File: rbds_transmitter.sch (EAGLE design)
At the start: 36 parts, among them IC1 MAX1551, IC2 TPS61030, IC3 MCP4812, Q1 P-Ch, SW1 FSMSM, U3 ATMEGA328, X1 HD44780LCD-1602, Y1 16Mhz

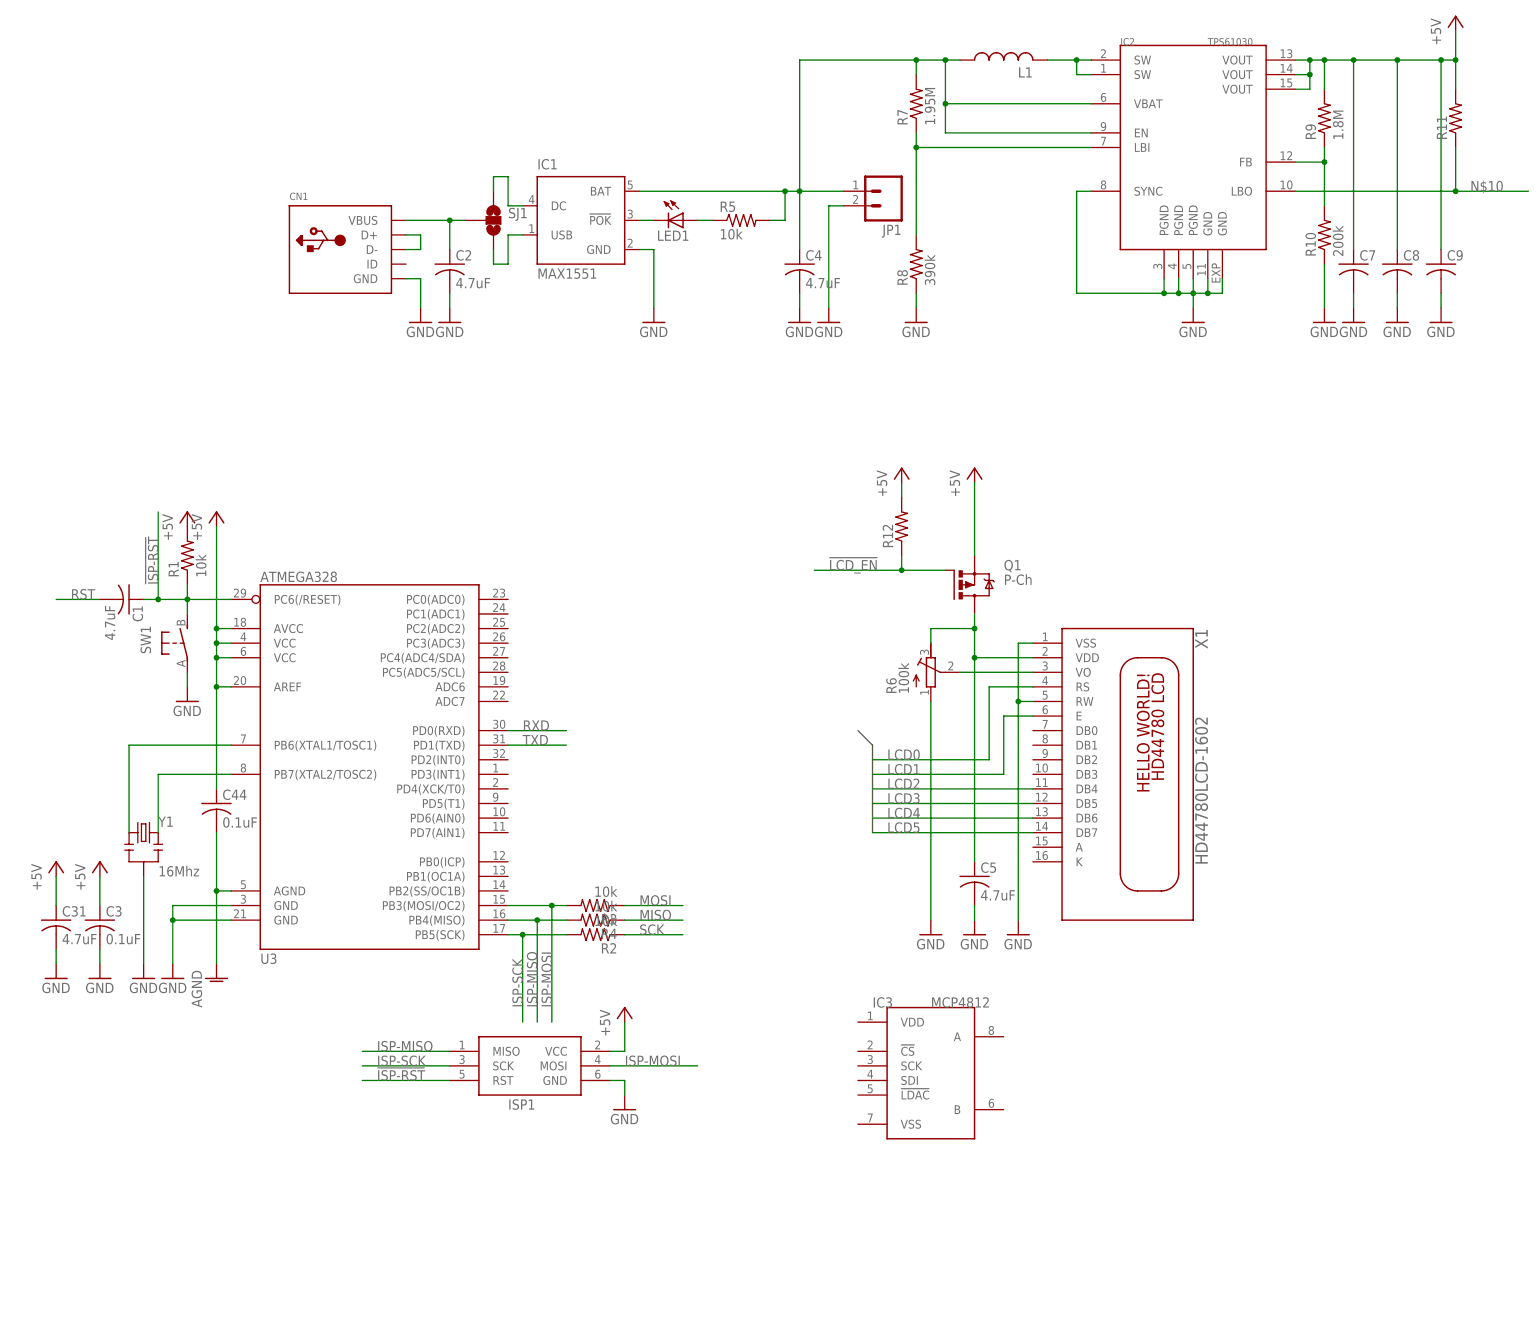
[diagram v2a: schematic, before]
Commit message: wiring up dac
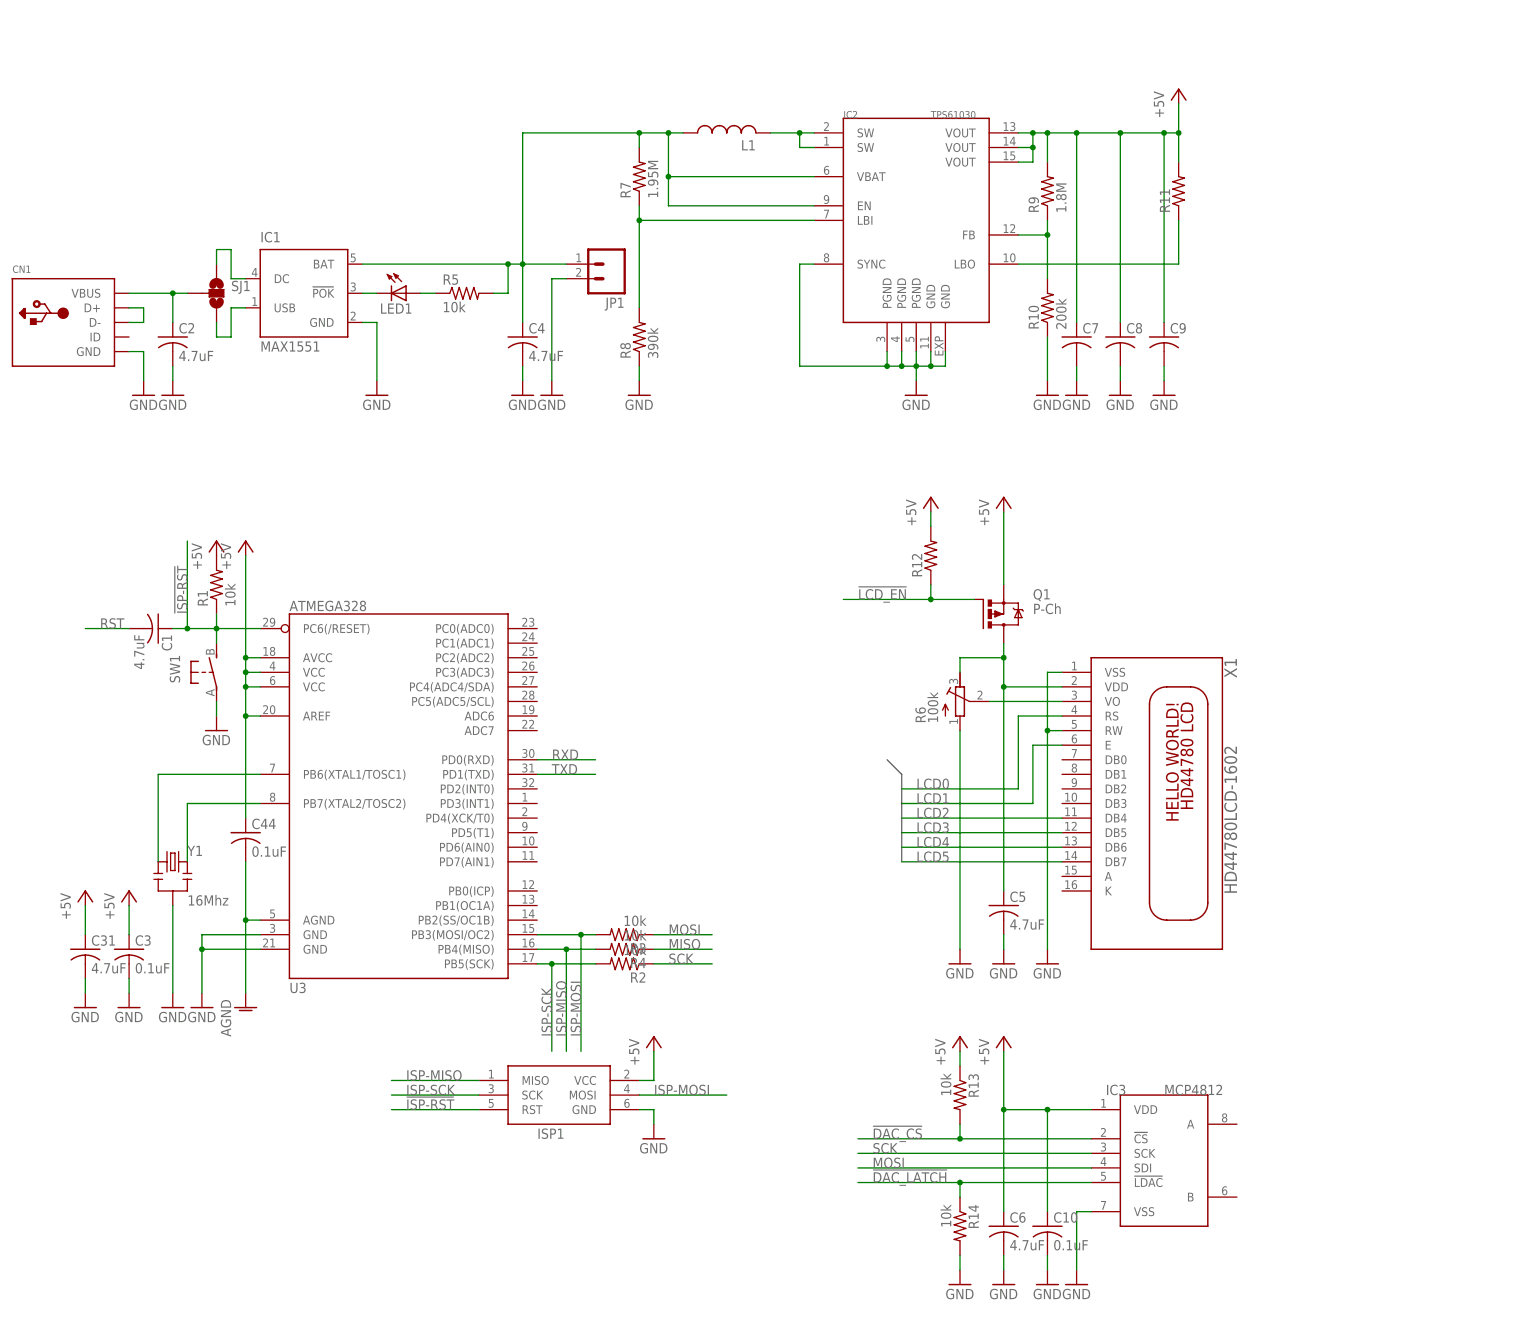
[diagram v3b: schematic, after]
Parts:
- added C10: 0.1uF, adafruit:C-USC1206
- added C6: 4.7uF, adafruit:C-USC1206
- added R13, R14: 10k, adafruit:R-US_R1206
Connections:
- new net !DAC_CS: IC3.!CS, R13.2
- new net !DAC_LATCH: IC3.!LDAC, R14.1
- net +5V: now also C10.1, C6.1, IC3.VDD, R13.1
- net GND: now also C10.2, C6.2, IC3.VSS, R14.2
- net MOSI: now also IC3.SDI
- net SCK: now also IC3.SCK
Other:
- moved on the sheet: C1, C2, C3, C31, C4, C44, C5, C7, C8, C9, CN1, IC1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

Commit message: added diode ring mixer
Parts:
- added C11: (no value), adafruit:C-USC1206
- added D1, D2, D3, D4: (no value), dp_devices:DIODE-SOD-123
- added JP2: (no value), sparkfun:M02PTH
- added R15: (no value), adafruit:R-US_R1206
- added TR1, TR2: (no value), inductor-neosid:SM-T4-2T
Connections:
- new net N$14: D1.A, D4.C, TR1.2
- new net N$16: D1.C, D2.A, TR2.2
- new net N$18: D2.C, D3.A, TR1.4
- new net N$19: TR1.3
- new net N$20: R15.1, TR1.1
- new net N$21: C11.1, TR2.1
- new net N$22: C11.2
- new net N$3: D3.C, D4.A, TR2.4
- net GND: now also JP2.2, TR1.5, TR2.3, TR2.5
- net N$11: now also JP2.1

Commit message: opamps
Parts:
- added IC4: OPA4743UA, linear:OPA4743UA
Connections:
- net N$22: now also IC4A.+IN
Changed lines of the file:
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@@
 <grid distance="0.1" unitdist="inch" unit="inch" style="lines" multiple="1" display="no" altdistance="0.01" altunitdist="inch" altunit="inch"/>
 <layers>
-<layer number="1" name="Top" color="4" fill="1" visible="yes" active="no"/>
-<layer number="2" name="Route2" color="1" fill="3" visible="yes" active="no"/>
-<layer number="3" name="Route3" color="4" fill="3" visible="yes" active="no"/>
-<layer number="4" name="Route4" color="1" fill="4" visible="yes" active="no"/>
-<layer number="5" name="Route5" color="4" fill="4" visible="yes" active="no"/>
-<layer number="6" name="Route6" color="1" fill="8" visible="yes" active="no"/>
-<layer number="7" name="Route7" color="4" fill="8" visible="yes" active="no"/>
-<layer number="8" name="Route8" color="1" fill="2" visible="yes" active="no"/>
-<layer number="9" name="Route9" color="4" fill="2" visible="yes" active="no"/>
-<layer number="10" name="Route10" color="1" fill="7" visible="yes" active="no"/>
-<layer number="11" name="Route11" color="4" fill="7" visible="yes" active="no"/>
-<layer number="12" name="Route12" color="1" fill="5" visible="yes" active="no"/>
-<layer number="13" name="Route13" color="4" fill="5" visible="yes" active="no"/>
-<layer number="14" name="Route14" color="1" fill="6" visible="yes" active="no"/>
-<layer number="15" name="Route15" color="4" fill="6" visible="yes" active="no"/>
-<layer number="16" name="Bottom" color="1" fill="1" visible="yes" active="no"/>
-<layer number="17" name="Pads" color="2" fill="1" visible="yes" active="no"/>
-<layer number="18" name="Vias" color="2" fill="1" visible="yes" active="no"/>
-<layer number="19" name="Unrouted" color="6" fill="1" visible="yes" active="no"/>
-<layer number="20" name="Dimension" color="15" fill="1" visible="yes" active="no"/>
-<layer number="21" name="tPlace" color="7" fill="1" visible="yes" active="no"/>
-<layer number="22" name="bPlace" color="7" fill="1" visible="yes" active="no"/>
-<layer number="23" name="tOrigins" color="15" fill="1" visible="yes" active="no"/>
-<layer number="24" name="bOrigins" color="15" fill="1" visible="yes" active="no"/>
-<layer number="25" name="tNames" color="7" fill="1" visible="yes" active="no"/>
-<layer number="26" name="bNames" color="7" fill="1" visible="yes" active="no"/>
-<layer number="27" name="tValues" color="7" fill="1" visible="yes" active="no"/>
-<layer number="28" name="bValues" color="7" fill="1" visible="yes" active="no"/>
+<layer number="1" name="Top" color="4" fill="1" visible="no" active="no"/>
+<layer number="2" name="Route2" color="1" fill="3" visible="no" active="no"/>
+<layer number="3" name="Route3" color="4" fill="3" visible="no" active="no"/>
+<layer number="4" name="Route4" color="1" fill="4" visible="no" active="no"/>
+<layer number="5" name="Route5" color="4" fill="4" visible="no" active="no"/>
+<layer number="6" name="Route6" color="1" fill="8" visible="no" active="no"/>
+<layer number="7" name="Route7" color="4" fill="8" visible="no" active="no"/>
+<layer number="8" name="Route8" color="1" fill="2" visible="no" active="no"/>
+<layer number="9" name="Route9" color="4" fill="2" visible="no" active="no"/>
+<layer number="10" name="Route10" color="1" fill="7" visible="no" active="no"/>
+<layer number="11" name="Route11" color="4" fill="7" visible="no" active="no"/>
+<layer number="12" name="Route12" color="1" fill="5" visible="no" active="no"/>
+<layer number="13" name="Route13" color="4" fill="5" visible="no" active="no"/>
+<layer number="14" name="Route14" color="1" fill="6" visible="no" active="no"/>
+<layer number="15" name="Route15" color="4" fill="6" visible="no" active="no"/>
+<layer number="16" name="Bottom" color="1" fill="1" visible="no" active="no"/>
+<layer number="17" name="Pads" color="2" fill="1" visible="no" active="no"/>
+<layer number="18" name="Vias" color="2" fill="1" visible="no" active="no"/>
+<layer number="19" name="Unrouted" color="6" fill="1" visible="no" active="no"/>
+<layer number="20" name="Dimension" color="15" fill="1" visible="no" active="no"/>
+<layer number="21" name="tPlace" color="7" fill="1" visible="no" active="no"/>
+<layer number="22" name="bPlace" color="7" fill="1" visible="no" active="no"/>
+<layer number="23" name="tOrigins" color="15" fill="1" visible="no" active="no"/>
+<layer number="24" name="bOrigins" color="15" fill="1" visible="no" active="no"/>
+<layer number="25" name="tNames" color="7" fill="1" visible="no" active="no"/>
+<layer number="26" name="bNames" color="7" fill="1" visible="no" active="no"/>
+<layer number="27" name="tValues" color="7" fill="1" visible="no" active="no"/>
+<layer number="28" name="bValues" color="7" fill="1" visible="no" active="no"/>
 <layer number="29" name="tStop" color="7" fill="3" visible="no" active="no"/>
 <layer number="30" name="bStop" color="7" fill="6" visible="no" active="no"/>
@@
 <layer number="35" name="tGlue" color="7" fill="4" visible="no" active="no"/>
 <layer number="36" name="bGlue" color="7" fill="5" visible="no" active="no"/>
-<layer number="37" name="tTest" color="7" fill="1" visible="yes" active="no"/>
-<layer number="38" name="bTest" color="7" fill="1" visible="yes" active="no"/>
+<layer number="37" name="tTest" color="7" fill="1" visible="no" active="no"/>
+<layer number="38" name="bTest" color="7" fill="1" visible="no" active="no"/>
 <layer number="39" name="tKeepout" color="4" fill="11" visible="no" active="no"/>
 <layer number="40" name="bKeepout" color="1" fill="11" visible="no" active="no"/>
@@
 <layer number="44" name="Drills" color="7" fill="1" visible="no" active="no"/>
 <layer number="45" name="Holes" color="7" fill="1" visible="no" active="no"/>
-<layer number="46" name="Milling" color="3" fill="1" visible="yes" active="no"/>
-<layer number="47" name="Measures" color="7" fill="1" visible="yes" active="no"/>
-<layer number="48" name="Document" color="7" fill="1" visible="yes" active="no"/>
-<layer number="49" name="Reference" color="7" fill="1" visible="yes" active="no"/>
-<layer number="50" name="dxf" color="7" fill="1" visible="yes" active="no"/>
-<layer number="51" name="tDocu" color="7" fill="1" visible="yes" active="no"/>
-<layer number="52" name="bDocu" color="7" fill="1" visible="yes" active="no"/>
-<layer number="53" name="tGND_GNDA" color="7" fill="9" visible="yes" active="no"/>
-<layer number="54" name="bGND_GNDA" color="1" fill="9" visible="yes" active="no"/>
-<layer number="56" name="wert" color="7" fill="1" visible="yes" active="no"/>
-<layer number="57" name="tCAD" color="7" fill="1" visible="yes" active="no"/>
+<layer number="46" name="Milling" color="3" fill="1" visible="no" active="no"/>
+<layer number="47" name="Measures" color="7" fill="1" visible="no" active="no"/>
+<layer number="48" name="Document" color="7" fill="1" visible="no" active="no"/>
+<layer number="49" name="Reference" color="7" fill="1" visible="no" active="no"/>
+<layer number="50" name="dxf" color="7" fill="1" visible="no" active="no"/>
+<layer number="51" name="tDocu" color="7" fill="1" visible="no" active="no"/>
+<layer number="52" name="bDocu" color="7" fill="1" visible="no" active="no"/>
+<layer number="53" name="tGND_GNDA" color="7" fill="9" visible="no" active="no"/>
+<layer number="54" name="bGND_GNDA" color="1" fill="9" visible="no" active="no"/>
+<layer number="56" name="wert" color="7" fill="1" visible="no" active="no"/>
+<layer number="57" name="tCAD" color="7" fill="1" visible="no" active="no"/>
 <layer number="91" name="Nets" color="2" fill="1" visible="yes" active="yes"/>
 <layer number="92" name="Busses" color="1" fill="1" visible="yes" active="yes"/>
@@
 <part name="R15" library="adafruit" deviceset="R-US_" device="R1206"/>
 <part name="C11" library="adafruit" deviceset="C-US" device="C1206"/>
+<part name="IC4" library="linear" deviceset="OPA4743" device="UA"/>
 </parts>
 <sheets>
@@
 <instance part="R15" gate="G$1" x="241.3" y="-10.16" rot="R180"/>
 <instance part="C11" gate="G$1" x="289.56" y="-10.16" rot="R90"/>
+<instance part="IC4" gate="A" x="312.42" y="-12.7"/>
+<instance part="IC4" gate="B" x="368.3" y="5.08"/>
+<instance part="IC4" gate="C" x="261.62" y="15.24"/>
+<instance part="IC4" gate="D" x="284.48" y="15.24"/>
+<instance part="IC4" gate="P" x="284.48" y="33.02"/>
 </instances>
 <busses>
@@
 <segment>
 <pinref part="C11" gate="G$1" pin="2"/>
-<wire x1="294.64" y1="-10.16" x2="302.26" y2="-10.16" width="0.1524" layer="91"/>
-</segment>
-</net>
+<wire x1="294.64" y1="-10.16" x2="304.8" y2="-10.16" width="0.1524" layer="91"/>
+<pinref part="IC4" gate="A" pin="+IN"/>
+</segment>
+</net>
